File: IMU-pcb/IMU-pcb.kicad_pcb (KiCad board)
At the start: 2 copper layers, 76.8 x 41 mm, 13 parts, among them J1 Status Rails, J2 Battery, J3 AUX Sensor, U1 4056Board, U2 WeMos_D1_mini, U3 IMU Sensor

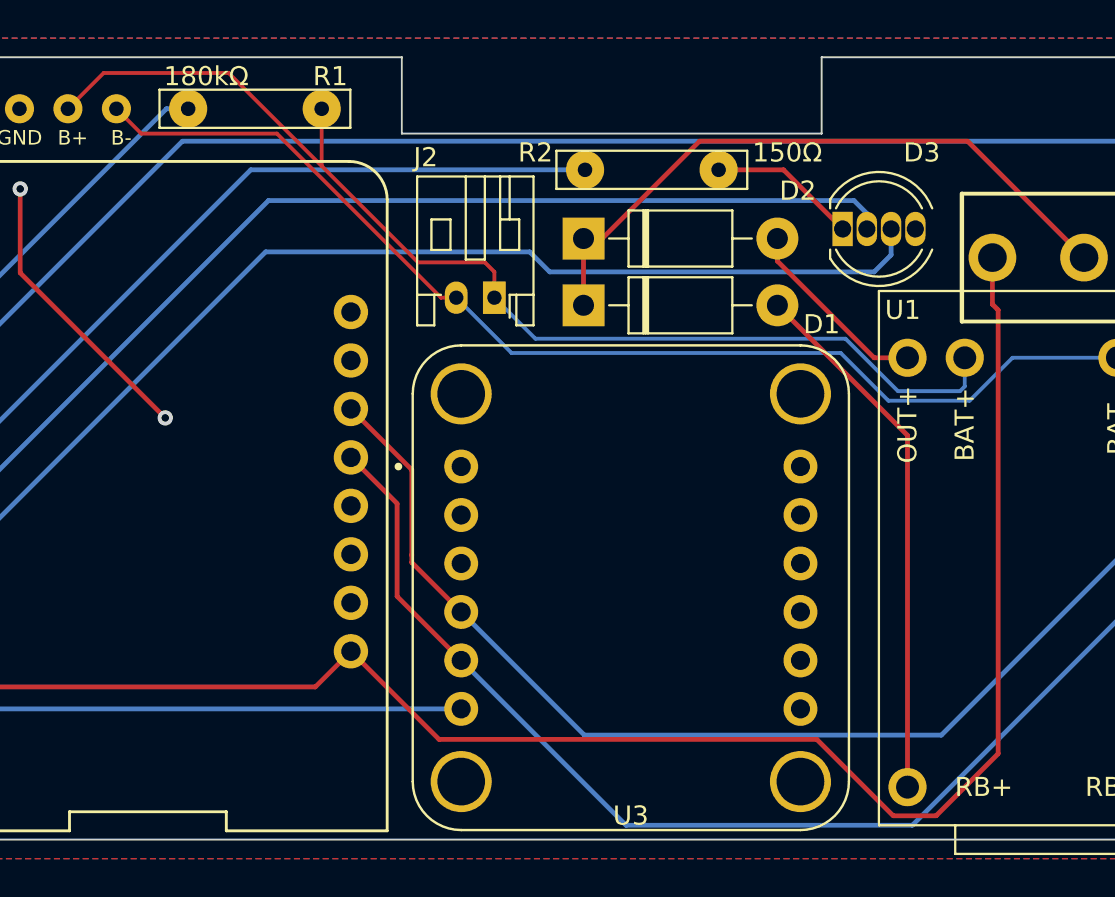
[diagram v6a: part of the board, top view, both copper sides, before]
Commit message: Adjusted pcb layout to be better
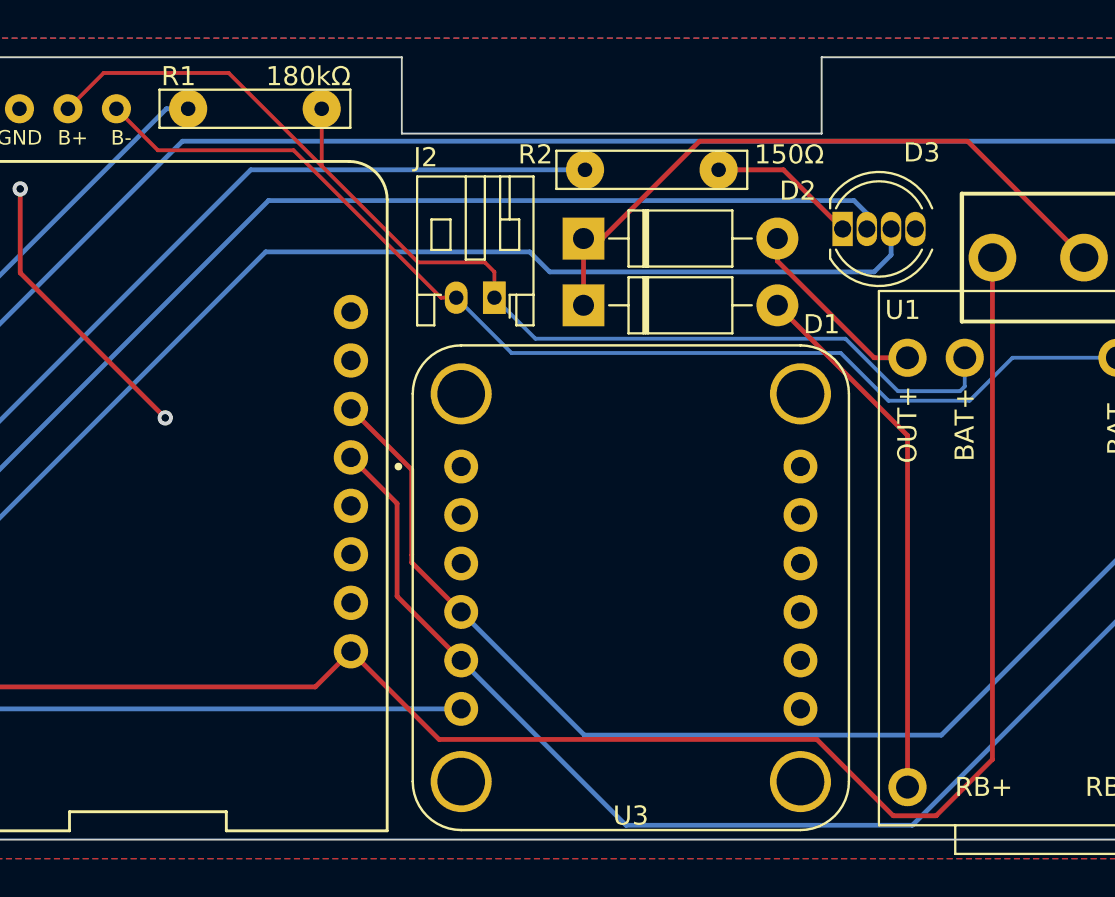
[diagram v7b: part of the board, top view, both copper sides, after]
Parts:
- R1: footprint PLANETS:180KΩ -> PLANETS:180KOhm
- R2: footprint PLANETS:150Ω -> PLANETS:150Ohm
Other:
- rule pad_to_mask_clearance: 0 -> 0.0508
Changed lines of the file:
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@@
       (dielectric_constraints no)
     )
-    (pad_to_mask_clearance 0)
+    (pad_to_mask_clearance 0.0508)
+    (solder_mask_min_width 0.101)
     (pcbplotparams
       (layerselection 0x00010fc_ffffffff)
@@
       (drillshape 0)
       (scaleselection 1)
-      (outputdirectory "../gerbers/")
+      (outputdirectory "C:/Users/angel/Desktop/IMU-pcb/gerbers_v1.1/")
     )
   )
@@
     )
   )
-  (footprint "PLANETS:150Ω" (layer "F.Cu")
+  (footprint "PLANETS:150Ohm" (layer "F.Cu")
     (at 151.1 74.9 -90)
     (property "Sheetfile" "IMU-pcb.kicad_sch")
     (property "Sheetname" "")
     (attr through_hole)
-    (fp_text reference "R2" (at -0.9 6.1) (layer "F.SilkS")
+    (fp_text reference "R2" (at -0.8 6.1) (layer "F.SilkS")
       (effects (font (size 1 1) (thickness 0.15)))
     )
-    (fp_text value "150" (at 0 6 90) (layer "F.Fab") hide
+    (fp_text value "150" (at 0 6 -90) (layer "F.Fab") hide
       (effects (font (size 1 1) (thickness 0.15)))
     )
-    (fp_text user "150Ω" (at -0.9 -7.1) (layer "F.SilkS")
+    (fp_text user "150Ω" (at -0.8 -7.2) (layer "F.SilkS")
       (effects (font (size 1 1) (thickness 0.15)))
     )
-    (fp_line (start 1 5) (end -1 5) (layer "F.SilkS") (width 0.12))
-    (fp_line (start 1 -5) (end 1 5) (layer "F.SilkS") (width 0.12))
     (fp_line (start -1 5) (end -1 -5) (layer "F.SilkS") (width 0.12))
+    (fp_line (start 1 -5) (end 1 5) (layer "F.SilkS") (width 0.12))
     (fp_line (start -1 -5) (end 1 -5) (layer "F.SilkS") (width 0.12))
+    (fp_line (start 1 5) (end -1 5) (layer "F.SilkS") (width 0.12))
     (pad "1" thru_hole circle (at 0 -3.5 270) (size 2 2) (drill 0.762) (layers *.Cu *.Mask)
       (net 7 "Net-(D3-Pad1)") (pintype "passive"))
@@
       (net 29 "D6") (pintype "passive"))
   )
-  (footprint "PLANETS:180KΩ" (layer "F.Cu")
+  (footprint "PLANETS:180KOhm" (layer "F.Cu")
     (at 130.3 71.7 -90)
     (property "Sheetfile" "IMU-pcb.kicad_sch")
@@
     (property "Spice_Primitive" "R")
     (attr through_hole)
-    (fp_text reference "R1" (at -1.7 -3.95) (layer "F.SilkS")
+    (fp_text reference "R1" (at -1.7 4) (layer "F.SilkS")
       (effects (font (size 1 1) (thickness 0.15)))
     )
@@
       (effects (font (size 1 1) (thickness 0.15)))
     )
-    (fp_text user "180kΩ" (at -1.7 2.55) (layer "F.SilkS")
+    (fp_text user "180kΩ" (at -1.7 -2.8) (layer "F.SilkS")
       (effects (font (size 1 1) (thickness 0.15)))
     )
-    (fp_line (start -1 5) (end -1 -5) (layer "F.SilkS") (width 0.12))
     (fp_line (start 1 5) (end -1 5) (layer "F.SilkS") (width 0.12))
-    (fp_line (start -1 -5) (end 1 -5) (layer "F.SilkS") (width 0.12))
+    (fp_line (start -1 5) (end -1 -5) (layer "F.SilkS") (width 0.12))
     (fp_line (start 1 -5) (end 1 5) (layer "F.SilkS") (width 0.12))
+    (fp_line (start -1 -5) (end 1 -5) (layer "F.SilkS") (width 0.12))
     (pad "1" thru_hole circle locked (at 0 -3.5 270) (size 2 2) (drill 0.762) (layers *.Cu *.Mask)
       (net 1 "B+") (pintype "passive"))
@@
   (segment (start 145 83.75) (end 142.85 81.6) (width 0.2) (layer "B.Cu") (net 1))
   (segment (start 140.85 81.6) (end 140.05 81.6) (width 0.2) (layer "F.Cu") (net 2))
-  (segment (start 124.34 73) (end 123.04 71.7) (width 0.2) (layer "F.Cu") (net 2))
-  (segment (start 140.05 81.6) (end 131.45 73) (width 0.2) (layer "F.Cu") (net 2))
-  (segment (start 131.45 73) (end 124.34 73) (width 0.2) (layer "F.Cu") (net 2))
+  (segment (start 125.215 73.875) (end 132.325 73.875) (width 0.2) (layer "F.Cu") (net 2))
+  (segment (start 140.05 81.6) (end 132.325 73.875) (width 0.2) (layer "F.Cu") (net 2))
+  (segment (start 123.04 71.7) (end 125.215 73.875) (width 0.2) (layer "F.Cu") (net 2))
   (segment (start 167.75 87) (end 163.5 87) (width 0.2) (layer "B.Cu") (net 2))
   (segment (start 163.5 87) (end 161 84.5) (width 0.2) (layer "B.Cu") (net 2))
@@
   (via (at 125.6 87.9) (size 0.8) (drill 0.4) (layers "F.Cu" "B.Cu") (free) (net 22))
   (via (at 118 75.9) (size 0.8) (drill 0.4) (layers "F.Cu" "B.Cu") (free) (net 22))
-  (segment (start 168.95 81.95) (end 168.95 79.5) (width 0.25) (layer "F.Cu") (net 24))
+  (segment (start 159.75 104.75) (end 139.95 104.75) (width 0.25) (layer "F.Cu") (net 24))
   (segment (start 112.25 102) (end 111 100.75) (width 0.25) (layer "F.Cu") (net 24))
-  (segment (start 169.25 82.25) (end 168.95 81.95) (width 0.25) (layer "F.Cu") (net 24))
-  (segment (start 139.95 104.75) (end 159.75 104.75) (width 0.25) (layer "F.Cu") (net 24))
-  (segment (start 169.25 105.5) (end 169.25 82.25) (width 0.25) (layer "F.Cu") (net 24))
+  (segment (start 163.75 108.75) (end 159.75 104.75) (width 0.25) (layer "F.Cu") (net 24))
+  (segment (start 168.95 79.5) (end 168.95 105.8) (width 0.25) (layer "F.Cu") (net 24))
+  (segment (start 168.95 105.8) (end 166 108.75) (width 0.25) (layer "F.Cu") (net 24))
   (segment (start 133.462024 102) (end 112.25 102) (width 0.25) (layer "F.Cu") (net 24))
   (segment (start 111 100.75) (end 111 81.75) (width 0.25) (layer "F.Cu") (net 24))
-  (segment (start 166 108.75) (end 169.25 105.5) (width 0.25) (layer "F.Cu") (net 24))
-  (segment (start 135.331012 100.131012) (end 139.95 104.75) (width 0.25) (layer "F.Cu") (net 24))
+  (segment (start 139.95 104.75) (end 135.331012 100.131012) (width 0.25) (layer "F.Cu") (net 24))
   (segment (start 111 81.75) (end 112.88 79.87) (width 0.25) (layer "F.Cu") (net 24))
-  (segment (start 159.75 104.75) (end 163.75 108.75) (width 0.25) (layer "F.Cu") (net 24))
-  (segment (start 163.75 108.75) (end 166 108.75) (width 0.25) (layer "F.Cu") (net 24))
   (segment (start 112.88 79.87) (end 112.88 71.7) (width 0.25) (layer "F.Cu") (net 24))
+  (segment (start 166 108.75) (end 163.75 108.75) (width 0.25) (layer "F.Cu") (net 24))
   (segment (start 135.331012 100.131012) (end 133.462024 102) (width 0.25) (layer "F.Cu") (net 24))
   (segment (start 130.082024 74.9) (end 112.471012 92.511012) (width 0.25) (layer "B.Cu") (net 29))
